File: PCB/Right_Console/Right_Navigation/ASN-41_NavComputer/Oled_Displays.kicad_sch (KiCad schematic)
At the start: 17 parts, among them U10 ER_OLEDM0.91_1x-I2C, U11 ER_OLEDM0.91_1x-I2C, U4 TCA9548APWR, U5 ER_OLEDM0.91_1x-I2C, U6 ER_OLEDM0.91_1x-I2C, U7 ER_OLEDM0.91_1x-I2C, U8 ER_OLEDM0.91_1x-I2C, U9 ER_OLEDM0.91_1x-I2C

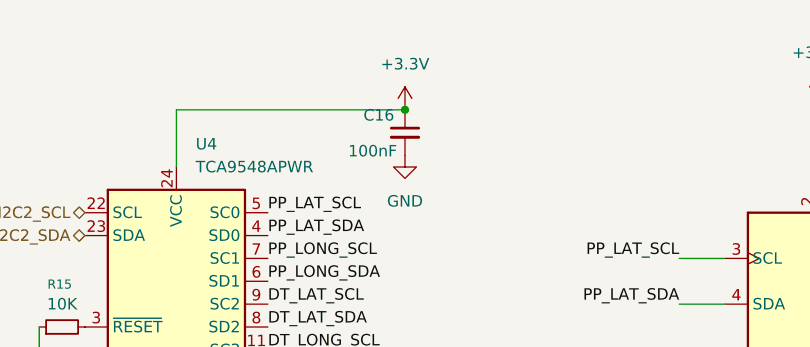
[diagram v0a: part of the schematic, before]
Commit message: feat(pcb): label LCSC/tolerance/voltage on Right_Nav + PDU schematics
Populate LCSC, Tolerance, and Rating (voltage/power) fields across the four
fabbed boards, sourced from InvenTree + the board tickets and PDU DESIGN-NOTES.
Values corrected to the selected part (100nF 50V, resistors 1%, AMS1117
C6186 -> C347222, 10uF split 25V/35V by +12V rail).

- PDU: dividers 0.1% (C2828767/C865184/C406725/C110774), J1 Mini-Fit 4-pin
  C20608114, D3/D4 green, C9 35V on +12V (SMBJ12A clamp margin).
- ARC-51A: MCP23017 C506653, TCA9548 C130026, J9 XH-8 C23067548, backlight
  J8 Mini-Fit 2-pin C20608113.
- ASN-41: AMS1117 C347222, TCA9548 C130026, 10uF per-rail split, 74HC165 x4
  C22384789, 1k ADC filter C844939, backlight J8 C20608113.
- APN-153: footprints (0805 passives + XH/Mini-Fit connectors) + MCP23017
  C506653, DRV8833 C50506, 2N7002 C8545, 2.2uF C87994 (25V X5R), 10nF C1710,
  6-pin XH J2 C23067546.

Off-board panel controls (encoders, rotary switches, OLED, pot, stepper, MEM
button) excluded as connector-coupled. Pin headers (SWD, CAN_TERM) hand-
soldered, no assembly LCSC. Harness mating ends tracked in the order BOM.
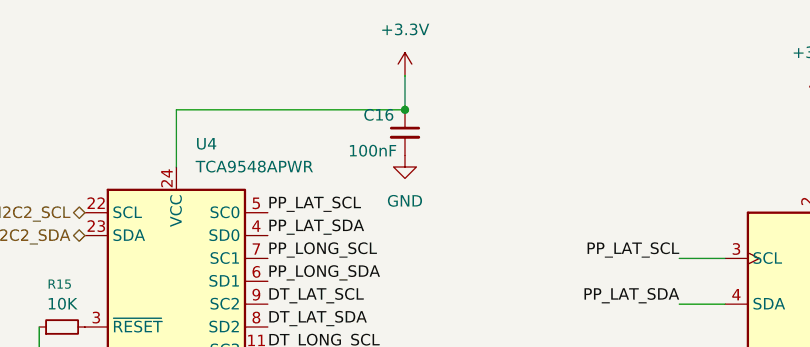
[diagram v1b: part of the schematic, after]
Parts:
- C16, C17, C18, C19, C20, C21, C22, C23: LCSC (none) -> C1711; Rating 16V -> 50V
- R15: LCSC (none) -> C844937; Tolerance 5% -> 1%

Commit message: chore(pcb): normalize passive value-string case fleet-wide
Cosmetic cleanup — standardize resistor/cap value strings so identical
parts stop showing as separate BOM lines. Value = magnitude only;
tolerance + LCSC carry the precision distinction.

- 10K -> 10k, 4.7K -> 4.7k, 100K -> 100k (lowercase SI k)
- 100nf -> 100nF
- 69 symbols across all 6 boards (ASN-41, ARC-51A, APN-153, PDU,
  Gateway_Bridge, PanelGroup_Base). ERC 0/0 on all.

No functional/footprint/LCSC change. PDU generic 10k and precision
divider 10k now both read "10k", distinguished by tolerance (1% vs 0.1%).
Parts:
- R15: value 10K -> 10k
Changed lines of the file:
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@@
 			)
 		)
-		(property "Value" "10K"
+		(property "Value" "10k"
 			(at 35.56 58.42 90)
 			(show_name no)

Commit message: feat(pcb): add descriptive IPN field to all on-board symbols (#238 Phase 3) (#239)
Phase 3 of the IPN convention (#238): adds a stable, descriptive
**Internal Part Number** to every on-board symbol, co-equal with LCSC.
BOMs now anchor on a fixed identity; the LCSC can change with
availability without altering the part's identity.

## What changed
- **352 symbols** across all 6 boards (multi-sheet aware) get an `IPN`
field. **51 distinct IPNs.** ERC clean fleet-wide.
- **Off-board controls** (encoders/switches/pots/OLED/stepper — no
footprint, connector-coupled) get **no IPN**, per the standing off-board
exclusion. On-board modules (RP2040-ZERO) and the RESET tact switch
**do** get IPNs.
- `.gitignore`: FreeCAD backups (`*.FCBak`/`*.FCStd1`) + KiCad ERC/DRC
reports (`*-erc.rpt`/`*-drc.rpt`).

## Scheme (descriptive, locked in #238)
`RES-10K-1PCT-0805` · `CAP-CER-100NF-50V-0805` · `CAP-ELEC-22UF-16V-D4`
· `IC-STM32F103C8-LQFP` · `CONN-XH-8P` · `TVS-SMBJ12A-SMB` ·
`FUSE-HOLDER-BLADE-DIP4` · `SW-TACT-6MM` · `MOD-RP2040-ZERO`.

Resolved the 3 open encoding items: ferrite → `FB-600R-0805` (TDK
600Ω@100MHz), NTC → `NTC-10K-1206` (APV 10K), fuse holder (C19727305 is
a *holder*, not a fuse) → one `FUSE-HOLDER-BLADE-DIP4`.

## Not in this PR (later phases of #238)
- **Phase 2 — InvenTree:** set the IPN field + link SupplierParts incl
backorder alternates (one IPN → many LCSC). This is what actually
delivers the churn-proofing; needs reviewed InvenTree writes.
- **Phase 4 — order flow:** resolve IPN → in-stock LCSC at order time.

Refs #238.
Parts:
- C16, C17, C18, C19, C20, C21, C22, C23: IPN (none) -> CAP-CER-100NF-50V-0805
- R15: IPN (none) -> RES-10K-1PCT-0805
- U4: IPN (none) -> IC-TCA9548A-SSOP
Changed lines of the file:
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@@
 			)
 		)
+		(property "IPN" "CAP-CER-100NF-50V-0805"
+			(at 260.35 40.64 0)
+			(hide yes)
+			(show_name no)
+			(do_not_autoplace no)
+			(effects
+				(font
+					(size 1.27 1.27)
+				)
+			)
+		)
 		(property "Description" "Unpolarized capacitor, small symbol"
 			(at 260.35 40.64 0)
@@
 			)
 		)
+		(property "IPN" "CAP-CER-100NF-50V-0805"
+			(at 198.12 39.37 0)
+			(hide yes)
+			(show_name no)
+			(do_not_autoplace no)
+			(effects
+				(font
+					(size 1.27 1.27)
+				)
+			)
+		)
 		(property "Description" "Unpolarized capacitor, small symbol"
 			(at 198.12 39.37 0)
@@
 			)
 		)
+		(property "IPN" "CAP-CER-100NF-50V-0805"
+			(at 73.66 39.37 0)
+			(hide yes)
+			(show_name no)
+			(do_not_autoplace no)
+			(effects
+				(font
+					(size 1.27 1.27)
+				)
+			)
+		)
 		(property "Description" "Unpolarized capacitor, small symbol"
 			(at 73.66 39.37 0)
@@
 			)
 		)
+		(property "IPN" "RES-10K-1PCT-0805"
+			(at 35.56 60.96 0)
+			(hide yes)
+			(show_name no)
+			(do_not_autoplace no)
+			(effects
+				(font
+					(size 1.27 1.27)
+				)
+			)
+		)
 		(property "Description" "Resistor, small symbol"
 			(at 35.56 60.96 0)
@@
 			)
 		)
+		(property "IPN" "IC-TCA9548A-SSOP"
+			(at 49.53 59.69 0)
+			(hide yes)
+			(show_name no)
+			(do_not_autoplace no)
+			(effects
+				(font
+					(size 1.27 1.27)
+				)
+			)
+		)
 		(property "Description" "Low voltage 8-channel I2C switch with reset, TSSOP-24"
 			(at 48.26 66.04 0)
@@
 			)
 		)
+		(property "IPN" "CAP-CER-100NF-50V-0805"
+			(at 261.62 97.79 0)
+			(hide yes)
+			(show_name no)
+			(do_not_autoplace no)
+			(effects
+				(font
+					(size 1.27 1.27)
+				)
+			)
+		)
 		(property "Description" "Unpolarized capacitor, small symbol"
 			(at 261.62 97.79 0)
@@
 			)
 		)
+		(property "IPN" "CAP-CER-100NF-50V-0805"
+			(at 132.08 40.64 0)
+			(hide yes)
+			(show_name no)
+			(do_not_autoplace no)
+			(effects
+				(font
+					(size 1.27 1.27)
+				)
+			)
+		)
 		(property "Description" "Unpolarized capacitor, small symbol"
 			(at 132.08 40.64 0)
@@
 			)
 		)
+		(property "IPN" "CAP-CER-100NF-50V-0805"
+			(at 130.81 93.98 0)
+			(hide yes)
+			(show_name no)
+			(do_not_autoplace no)
+			(effects
+				(font
+					(size 1.27 1.27)
+				)
+			)
+		)
 		(property "Description" "Unpolarized capacitor, small symbol"
 			(at 130.81 93.98 0)
@@
 			)
 		)
+		(property "IPN" "CAP-CER-100NF-50V-0805"
+			(at 130.81 148.59 0)
+			(hide yes)
+			(show_name no)
+			(do_not_autoplace no)
+			(effects
+				(font
+					(size 1.27 1.27)
+				)
+			)
+		)
 		(property "Description" "Unpolarized capacitor, small symbol"
 			(at 130.81 148.59 0)
@@
 			(at 196.85 95.25 0)
 			(hide yes)
+			(show_name no)
+			(do_not_autoplace no)
+			(effects
+				(font
+					(size 1.27 1.27)
+				)
+			)
+		)
+		(property "IPN" "CAP-CER-100NF-50V-0805"
+			(at 196.85 95.25 0)
+			(hide yes)
